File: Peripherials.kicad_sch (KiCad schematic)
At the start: 32 parts, among them J13 USB_C_Receptacle_USB2.0_14P, J14 IDC_Cable_02x08, J15 Conn_01x02_Pin, J18 Micro_SD_Card, J26 Conn_01x08_Socket, J27 Conn_01x02_Socket, J9 Conn_01x08_Socket, Q2 NMOS, U13 USBLC6-2P6, U2 RV-3028-C7

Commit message: pwr
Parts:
- removed H1, H2, H3, H4: MountingHole, MountingHole:MountingHole_3.2mm_M3, symbol Mechanical:MountingHole
- removed J26, J9: Conn_01x08_Socket, Connector_PinHeader_2.54mm:PinHeader_1x08_P2.54mm_Vertical, symbol Connector:Conn_01x08_Socket
- removed J27: Conn_01x02_Socket, Connector_PinHeader_2.54mm:PinHeader_1x02_P2.54mm_Vertical, symbol Connector:Conn_01x02_Socket
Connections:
- no-connect marks 10 -> 3
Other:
- note removed: "ESP32 Mini Header"
- note removed: "Mounting Holes"
- note removed: "UART breakout"
- moved on the sheet: C22, C23, C24, C25, C41, C46, D6, D7, D8, J13, J14, J15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

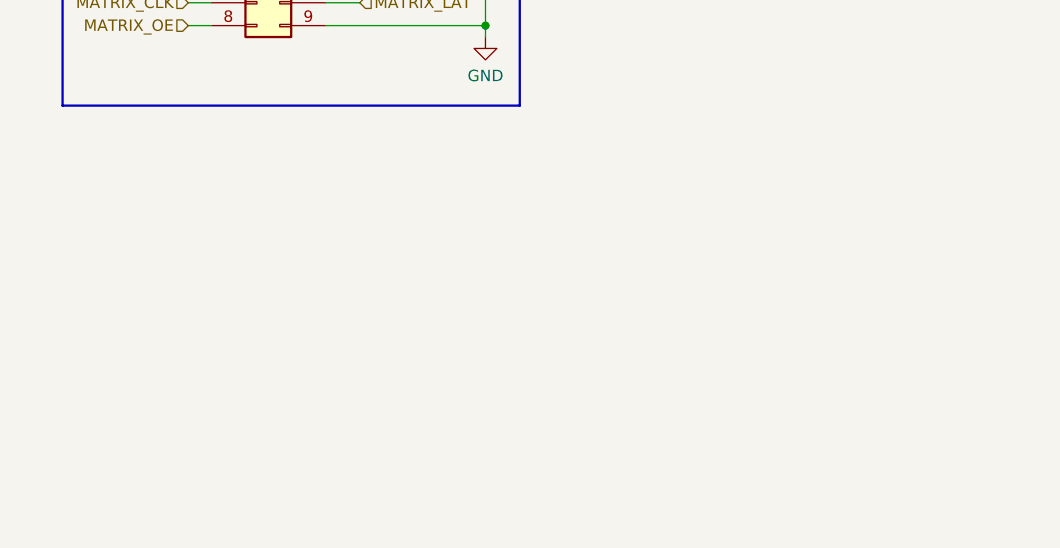
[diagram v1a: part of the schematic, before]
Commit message: added breakout for esp32 bluepill
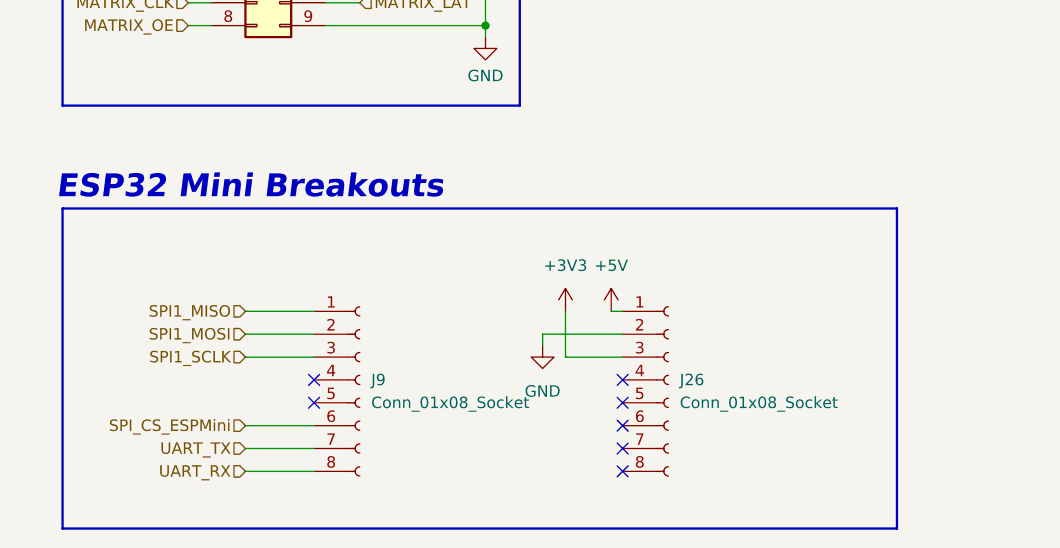
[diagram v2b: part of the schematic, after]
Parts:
- added J26, J9: Conn_01x08_Socket, Connector_PinHeader_2.54mm:PinHeader_1x08_P2.54mm_Vertical, symbol Connector:Conn_01x08_Socket
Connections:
- net GND: now also J26.2 (Pin_2)
- net SPI1_MISO: now also J9.1 (Pin_1)
- net SPI1_MOSI: now also J9.2 (Pin_2)
- net SPI1_SCLK: now also J9.3 (Pin_3)
- new net +3V3: J26.3 (Pin_3)
- new net +5V: J26.1 (Pin_1)
- new net SPI_CS_ESPMini: J9.6 (Pin_6)
- new net UART_RX: J9.8 (Pin_8)
- new net UART_TX: J9.7 (Pin_7)
- no-connect marks 3 -> 10
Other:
- note added: "ESP32 Mini Breakouts"

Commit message: mounting holes, hook up mini to stm32 g4
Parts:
- added H1, H2, H3, H4: MountingHole, MountingHole:MountingHole_3.2mm_M3, symbol Mechanical:MountingHole
- added J27: Conn_01x02_Socket, Connector_PinHeader_2.54mm:PinHeader_1x02_P2.54mm_Vertical, symbol Connector:Conn_01x02_Socket
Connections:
- net UART_RX renamed UART_RX_Mini
- net UART_RX_Mini: now also J27.2 (Pin_2)
- net UART_TX renamed UART_TX_Mini
- net UART_TX_Mini: now also J27.1 (Pin_1)
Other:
- note added: "ESP32 Mini Header"
- note added: "Mounting Holes"
- note added: "UART breakout"
- note removed: "ESP32 Mini Breakouts"
